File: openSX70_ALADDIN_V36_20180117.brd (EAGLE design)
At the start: 95.9 x 27.9 mm, 38 parts, among them Q1 5.8A/30V/35mΩ, Q2 5.8A/30V/35mΩ, U1 ATMEGA328P_TQFP, U3 BH1750FVI-TR, Y1 CSTCE16M0V53-R0

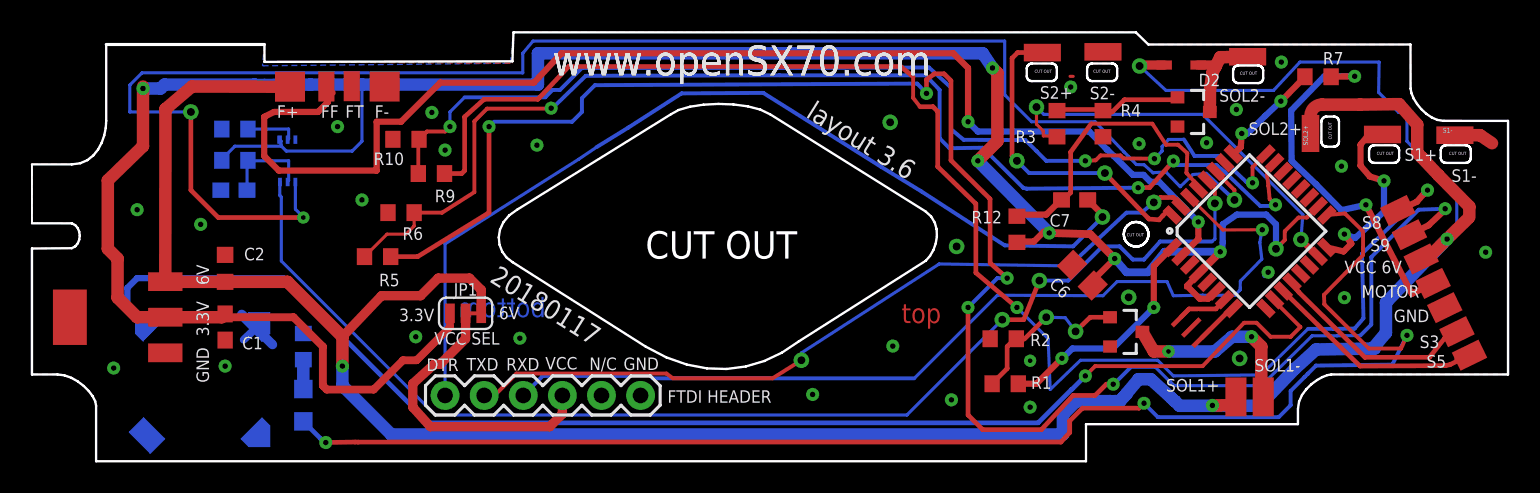
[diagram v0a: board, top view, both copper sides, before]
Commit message: Changed name on brd and version number.
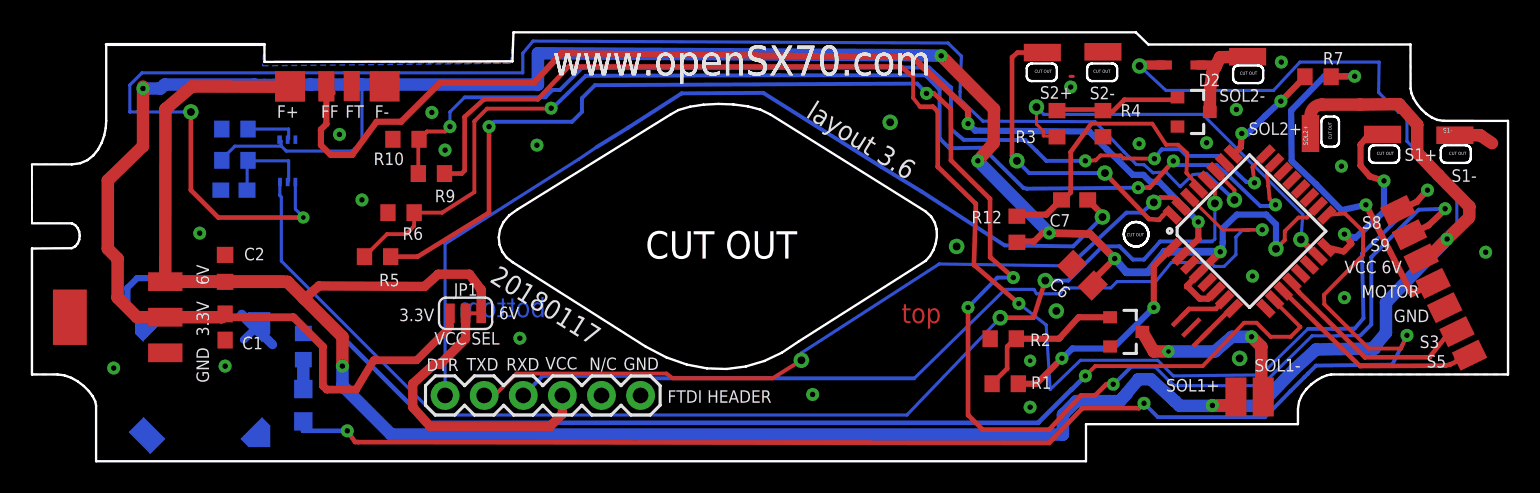
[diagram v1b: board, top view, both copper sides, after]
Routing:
- net FF: track 84.0 -> 72.4 mm
- net S9@6V: track 114.6 -> 112.5 mm
- net 3.3V: track 167.3 -> 165.6 mm
- net 6V: track 186.0 -> 187.7 mm
- net RXD: track 60.6 -> 59.4 mm
- net N$1: track 11.1 -> 10.3 mm, vias 2 -> 0
- net S8@3.3V: track 68.0 -> 67.4 mm
- net GND: track 8.20 -> 7.88 mm, vias 29 -> 25
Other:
- board text added: "openSX70 project visit www.openSX70.com version 3.6 "aladdin" 20170117 by Joaquín de Prada"
- board text removed: "openSX70 project visit www.openSX70.com version 3.6 "aladdin" 20170116 by Joaquín de Prada"

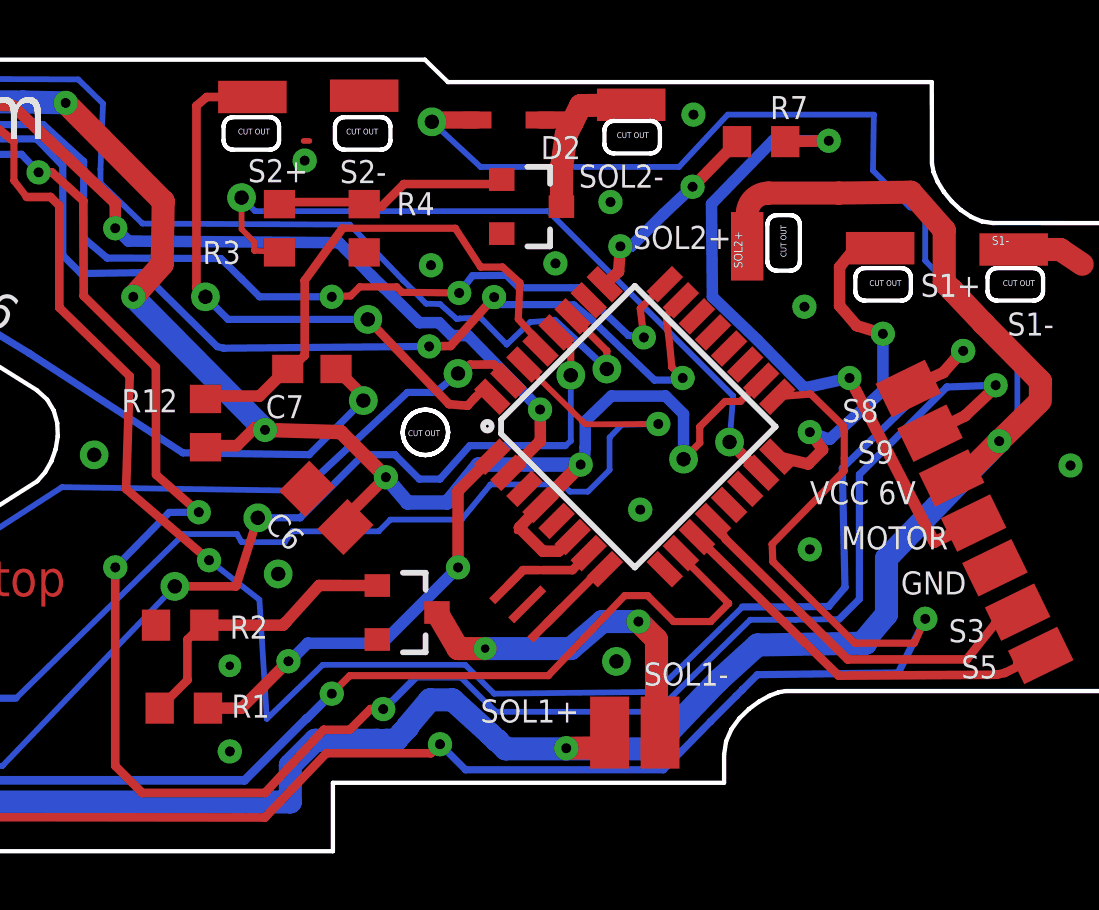
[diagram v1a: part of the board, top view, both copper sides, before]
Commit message: Added a protection diode D1 to solenoid#1 for protection. I had assumed that it was built in the solenoid but Phyvine Tong indicated that some later models (alpha) don't have it.
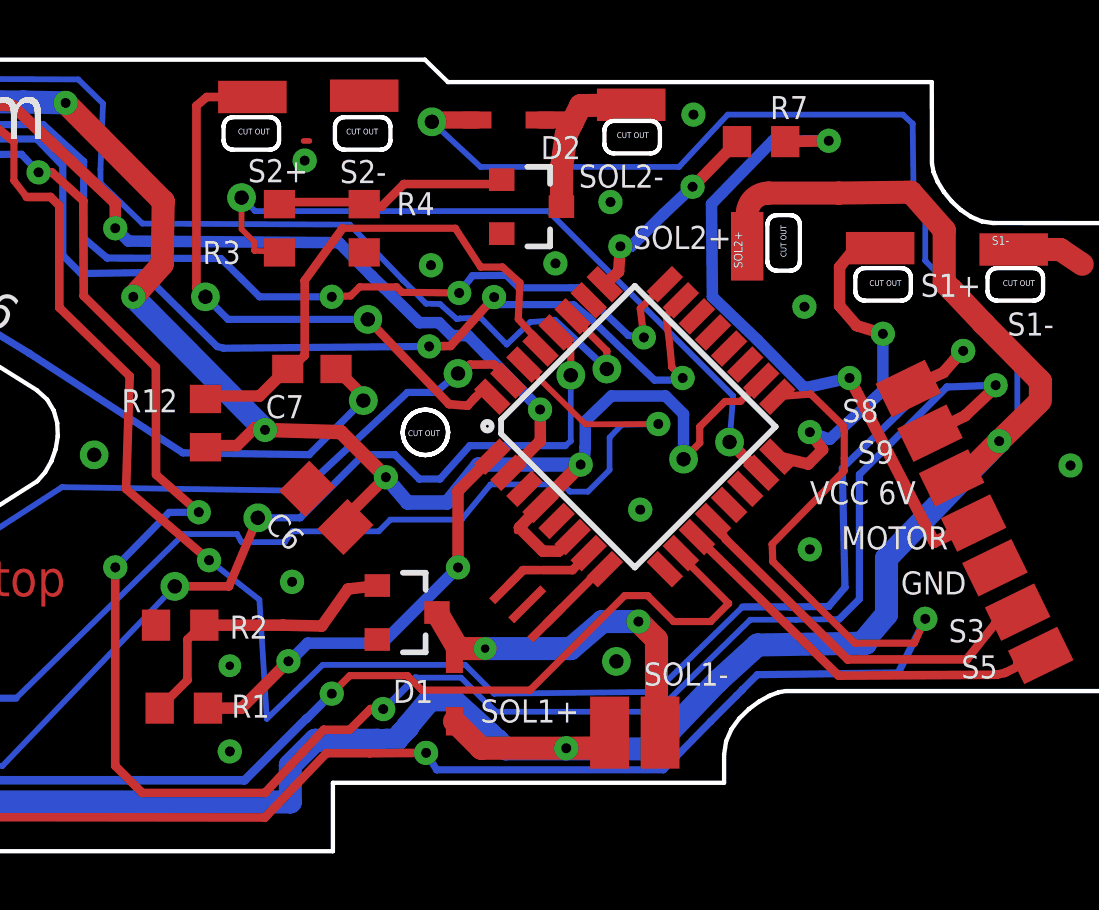
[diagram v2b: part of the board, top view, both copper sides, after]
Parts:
- added D1: 1N4148WSF, zetex:SOD323
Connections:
- net 6V: now also D1.1
- net SOL1-: now also D1.2
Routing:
- net 6V: track 187.7 -> 192.3 mm
- net SOL1-: track 12.4 -> 14.2 mm
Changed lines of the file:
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@@
 <attribute name="VALUE" x="30.226" y="9.271" size="0.6096" layer="27" font="vector" ratio="20" align="top-center"/>
+</element>
+<element name="D1" library="zetex" library_urn="urn:adsk.eagle:library:418" package="SOD323" package3d_urn="urn:adsk.eagle:package:30992/1" value="1N4148WSF" x="74.803" y="6.477" smashed="yes" rot="R90">
+<attribute name="MF" value="" x="74.803" y="6.477" size="1.778" layer="27" rot="R90" display="off"/>
+<attribute name="MPN" value="CDSOD323-T05C" x="74.803" y="6.477" size="1.778" layer="27" rot="R90" display="off"/>
+<attribute name="NAME" x="74.052" y="6.84" size="0.8128" layer="25" font="vector" ratio="20" rot="R180"/>
+<attribute name="OC_FARNELL" value="1824860" x="74.803" y="6.477" size="1.778" layer="27" rot="R90" display="off"/>
+<attribute name="OC_NEWARK" value="79R6078" x="74.803" y="6.477" size="1.778" layer="27" rot="R90" display="off"/>
+<attribute name="VALUE" x="76.608" y="5.577" size="1.016" layer="27" rot="R90"/>
 </element>
 </elements>
@@
 <wire x1="86.168225" y1="16.803425" x2="87.34425" y2="16.898675" width="0.254" layer="1"/>
 <via x="91.3765" y="8.98525" extent="1-16" drill="0.35"/>
-<wire x1="70.2945" y1="4.2545" x2="73.9775" y2="4.2545" width="0.3048" layer="1"/>
-<via x="74.295" y="4.572" extent="1-16" drill="0.35"/>
-<wire x1="74.295" y1="4.572" x2="75.1961" y2="3.6709" width="0.254" layer="16"/>
-<wire x1="73.9775" y1="4.2545" x2="74.295" y2="4.572" width="0.3048" layer="1"/>
-<wire x1="75.1961" y1="3.6709" x2="82.1569" y2="3.6709" width="0.254" layer="16"/>
+<wire x1="70.2945" y1="4.2545" x2="71.8185" y2="4.2545" width="0.3048" layer="1"/>
+<via x="73.80605" y="4.2672" extent="1-16" drill="0.35"/>
+<wire x1="73.80605" y1="4.2672" x2="74.1801" y2="3.6709" width="0.254" layer="16"/>
+<wire x1="71.8185" y1="4.2545" x2="73.80605" y2="4.2672" width="0.3048" layer="1"/>
+<wire x1="74.1801" y1="3.6709" x2="82.1569" y2="3.6709" width="0.254" layer="16"/>
 <wire x1="84.72074375" y1="6.27253125" x2="84.9359375" y2="6.48540625" width="0.254" layer="16"/>
 <wire x1="84.9359375" y1="6.48540625" x2="84.93595" y2="6.4877375" width="0.254" layer="16"/>
@@
 <wire x1="82.51659375" y1="8.89" x2="83.82" y2="8.89" width="0.254" layer="1"/>
 <wire x1="81.60499375" y1="9.8016" x2="82.51659375" y2="8.89" width="0.254" layer="1"/>
-<wire x1="80.7946" y1="9.8016" x2="78.105" y2="6.985" width="0.254" layer="1"/>
+<wire x1="80.7946" y1="9.8016" x2="77.47" y2="6.477" width="0.254" layer="1"/>
 <wire x1="80.7946" y1="9.8016" x2="81.60499375" y2="9.8016" width="0.254" layer="1"/>
 <wire x1="83.82" y1="8.89" x2="84.455" y2="9.525" width="0.254" layer="1"/>
 <wire x1="84.455" y1="9.525" x2="82.7741125" y2="11.2058875" width="0.254" layer="1"/>
 <wire x1="82.7741125" y1="11.2058875" x2="82.7741125" y2="11.298459375" width="0.3048" layer="1"/>
-<wire x1="71.12" y1="6.985" x2="78.105" y2="6.985" width="0.254" layer="1"/>
+<wire x1="71.12" y1="6.985" x2="73.152" y2="6.985" width="0.254" layer="1"/>
+<wire x1="73.152" y1="6.985" x2="73.66" y2="6.477" width="0.254" layer="1"/>
+<wire x1="73.66" y1="6.477" x2="77.47" y2="6.477" width="0.254" layer="1"/>
 <via x="70.485" y="6.35" extent="1-16" drill="0.35"/>
 <wire x1="69.589525" y1="5.4743" x2="69.6093" y2="5.4743" width="0.3048" layer="16"/>
@@
 <via x="62.12205" y="14.7574" extent="1-16" drill="0.508"/>
 <via x="80.5053" y="7.48665" extent="1-16" drill="0.508"/>
-<via x="68.59905" y="10.5664" extent="1-16" drill="0.508"/>
 <via x="12.954" y="15.621" extent="1-16" drill="0.35"/>
+<via x="69.088" y="10.287" extent="1-16" drill="0.35"/>
 </signal>
 <signal name="6V">
@@
 <wire x1="82.70875" y1="24.892" x2="75.72375" y2="24.892" width="0.2032" layer="16"/>
 <wire x1="84.42325" y1="26.7335" x2="82.70875" y2="24.892" width="0.2032" layer="16"/>
-<wire x1="89.56675" y1="26.7335" x2="84.42325" y2="26.7335" width="0.2032" layer="16"/>
-<wire x1="91.3765" y1="23.46325" x2="90.83675" y2="23.46325" width="0.2032" layer="16"/>
-<wire x1="90.83675" y1="23.46325" x2="89.535" y2="24.765" width="0.2032" layer="16"/>
-<wire x1="89.535" y1="24.765" x2="89.56675" y2="26.7335" width="0.2032" layer="16"/>
+<wire x1="90.58275" y1="26.7335" x2="84.42325" y2="26.7335" width="0.2032" layer="16"/>
+<wire x1="91.3765" y1="23.46325" x2="90.96375" y2="23.97125" width="0.2032" layer="16"/>
+<wire x1="90.96375" y1="23.97125" x2="90.932" y2="26.416" width="0.2032" layer="16"/>
+<wire x1="90.932" y1="26.416" x2="90.58275" y2="26.7335" width="0.2032" layer="16"/>
 <wire x1="91.3765" y1="21.59" x2="91.3765" y2="23.46325" width="0.2032" layer="16"/>
 <wire x1="94.615" y1="18.2245" x2="91.3765" y2="21.59" width="0.2032" layer="16"/>
@@
 <wire x1="27.560659375" y1="12.161315625" x2="20.701" y2="12.192" width="0.6096" layer="1"/>
 <wire x1="20.701" y1="12.192" x2="19.7485" y2="11.3665" width="0.6096" layer="1"/>
+<contactref element="D1" pad="1"/>
+<wire x1="74.803" y1="5.377" x2="75.7499" y2="4.4301" width="0.8128" layer="1"/>
+<wire x1="75.7499" y1="4.4301" x2="78.74" y2="4.4301" width="0.8128" layer="1"/>
 </signal>
 <signal name="SOL1-">
@@
 <wire x1="80.01" y1="8.89" x2="78.89875" y2="7.9375" width="0.8128" layer="16"/>
 <wire x1="78.89875" y1="7.9375" x2="75.8825" y2="7.9375" width="0.8128" layer="16"/>
+<contactref element="D1" pad="2"/>
+<wire x1="74.803" y1="7.577" x2="74.803" y2="8.339" width="0.4064" layer="1"/>
+<wire x1="74.803" y1="8.339" x2="74.1885" y2="9.2075" width="0.4064" layer="1"/>
 </signal>
 <signal name="N$1">
@@
 <contactref element="Q1" pad="1"/>
 <contactref element="R2" pad="2"/>
-<wire x1="70.0405" y1="10.16" x2="72.0885" y2="10.1575" width="0.4064" layer="1"/>
+<wire x1="71.0565" y1="10.033" x2="72.0885" y2="10.1575" width="0.4064" layer="1"/>
 <wire x1="65.405" y1="6.82625" x2="64.4525" y2="5.87375" width="0.3048" layer="1"/>
 <wire x1="65.405" y1="8.255" x2="65.405" y2="6.82625" width="0.3048" layer="1"/>
@@
 <wire x1="64.4525" y1="5.87375" x2="64.428" y2="5.842" width="0.2032" layer="1"/>
 <wire x1="65.88125" y1="8.73125" x2="66.001" y2="8.763" width="0.2032" layer="1"/>
-<wire x1="68.86575" y1="8.85825" x2="70.0405" y2="10.16" width="0.4064" layer="1"/>
+<wire x1="70.13575" y1="8.73125" x2="71.0565" y2="10.033" width="0.4064" layer="1"/>
 <wire x1="66.001" y1="8.763" x2="68.7705" y2="8.763" width="0.4064" layer="1"/>
-<wire x1="68.7705" y1="8.763" x2="68.86575" y2="8.85825" width="0.4064" layer="1"/>
+<wire x1="68.7705" y1="8.763" x2="70.13575" y2="8.73125" width="0.4064" layer="1"/>
 </signal>
 <signal name="N$3">
@@
 <wire x1="69.37375" y1="12.54125" x2="71.59625" y2="14.76375" width="0.254" layer="16"/>
 <wire x1="67.8815" y1="12.54125" x2="69.37375" y2="12.54125" width="0.254" layer="16"/>
-<wire x1="67.1195" y1="10.12825" x2="67.8815" y2="12.54125" width="0.3048" layer="1"/>
-<wire x1="64.9605" y1="10.12825" x2="67.1195" y2="10.12825" width="0.3048" layer="1"/>
+<wire x1="66.8655" y1="10.12825" x2="67.8815" y2="12.54125" width="0.3048" layer="1"/>
+<wire x1="64.9605" y1="10.12825" x2="66.8655" y2="10.12825" width="0.3048" layer="1"/>
 <wire x1="58.89625" y1="3.81" x2="64.9605" y2="10.12825" width="0.2032" layer="16"/>
 <wire x1="28.2575" y1="3.81" x2="58.89625" y2="3.81" width="0.2032" layer="16"/>

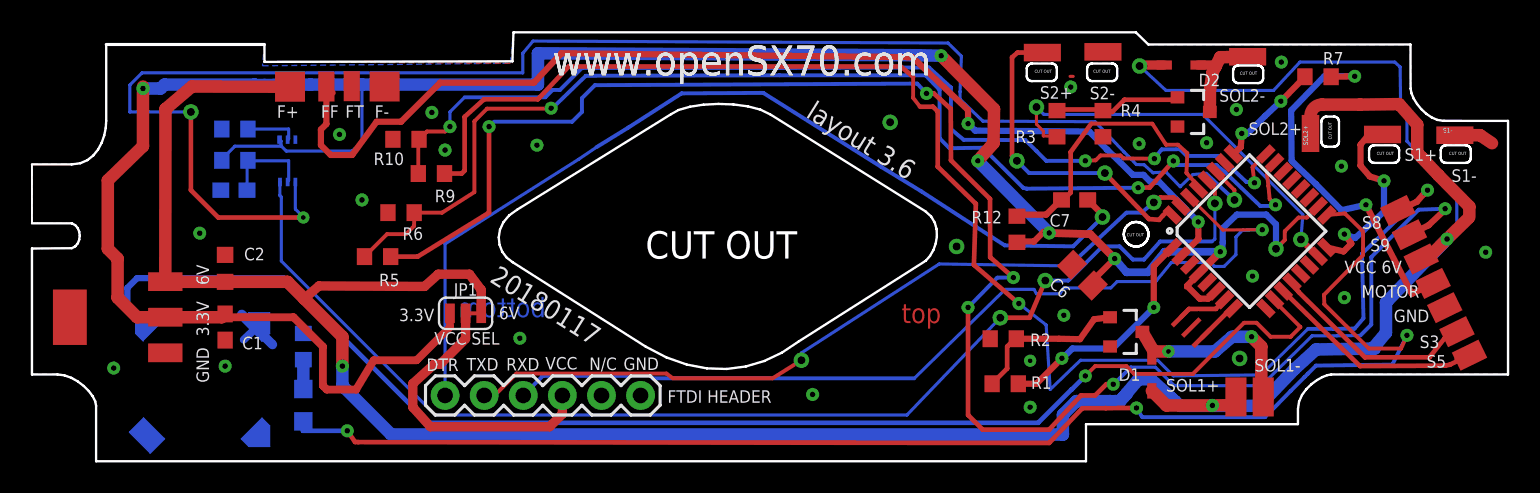
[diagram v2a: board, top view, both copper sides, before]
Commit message: Added GND 6V and 3.3V test points. Removed a bunch of innecessary vias.
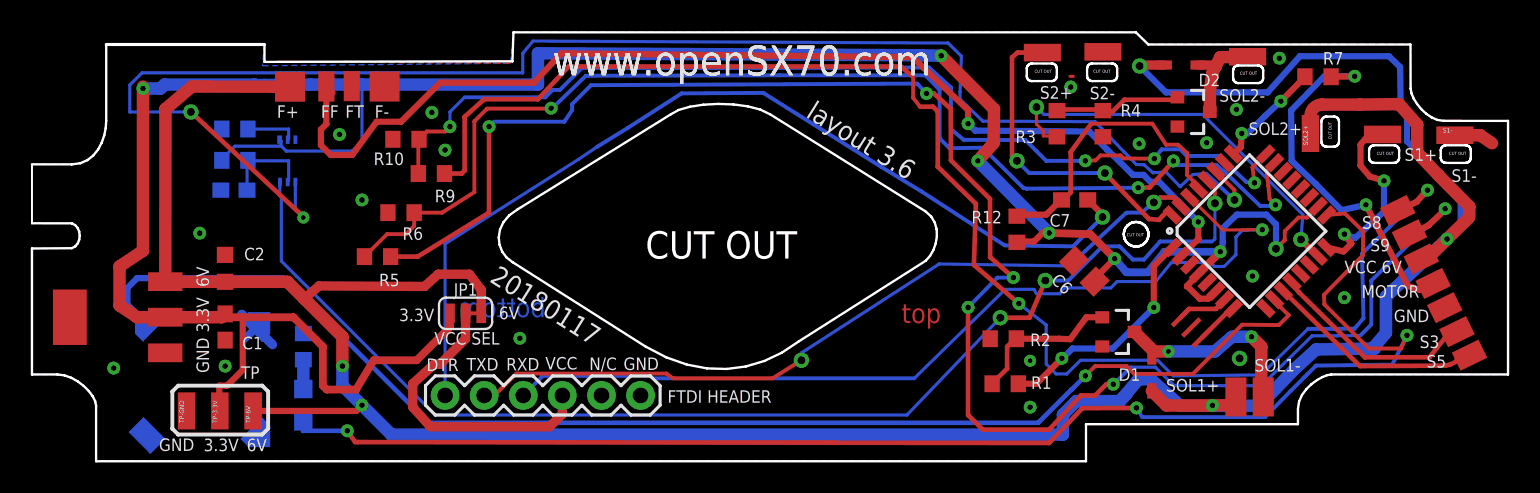
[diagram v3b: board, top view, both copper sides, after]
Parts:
- added TP-3.3V, TP-6V, TP-GND: SX70-S-PAD-NEW, openSX70:SX70-S-PAD2
- moved Q1 0.51 mm to (72.6, 9.21)
- moved C6 0.28 mm to (70.4, 13.1)
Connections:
- net 3.3V: now also TP-3.3V.P$1
- net 6V: now also TP-6V.P$1
- net GND: now also TP-GND.P$1
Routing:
- net 6V: track 192.3 -> 200.1 mm, vias 4 -> 5
- net 3.3V: track 165.6 -> 172.1 mm
- net SDA: track 104.1 -> 101.1 mm
- net BUZZER: track 90.7 -> 88.4 mm
- net S8@6V: track 95.9 -> 94.4 mm
- net S9@6V: track 112.5 -> 111.4 mm
- net SOL1-: track 14.2 -> 14.9 mm
- net GND: track 7.88 -> 8.06 mm, vias 25 -> 18
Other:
- board text added: "TP"

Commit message: I keep on tweaking compulsively. Definitely have to stop.
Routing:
- net 3.3V: track 172.1 -> 170.8 mm
- net 6V: track 200.1 -> 198.8 mm
- net SDA: track 101.1 -> 102.2 mm
- net GND: vias 18 -> 17
